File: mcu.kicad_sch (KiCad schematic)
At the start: 30 parts, among them SW1 RESET (RUN to GND), SW2 BOOTSEL (via R24), U20 RP2354B, Y1 12 MHz TAXM12M4RFBCCT2T, CL 1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

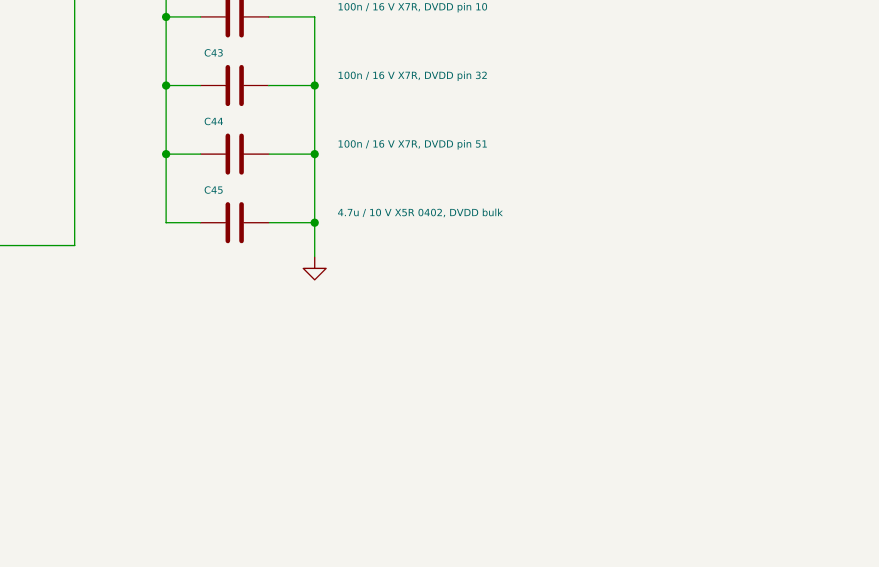
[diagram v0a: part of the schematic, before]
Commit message: Order-ready: core regulator per RP2350 §6.3.8, SWD header, second DVDD cap, README rewrite
Core regulator (U20 / C39 / C45 / L20):
- C39/C45 lands narrowed to 0.46 mm (0.50 mm gap) so VREG_LX passes between
  the pads as in datasheet Fig. 23; local 0.12 mm clearance rule for those
  two footprints only (inside JLC's 3.5 mil four-layer tier)
- In1 GND cutout under L20 and the LX net (Fig. 24); single-point ground
  return with two adjacent vias; B.Cu GND pour tying the SD-cluster vias
- L20 switched to the polarity-marked Abracon AOTA-B201610S3R3-101-T
  (LCSC C42411119) with a silk orientation dot at pad 2 / DVDD
- C81 added: second 4.7 uF on DVDD at the far edge of the package
- U22 BMP581: traces/vias moved out from under the body, mask window opened

Debug: J10 is now a 1x03 2.54 mm THT header wired SWCLK-GND-SWDIO
(Raspberry Pi Debug Probe order); checker, exporter, BOM sources and DFM
rules updated to match.

DFM: courtyard rules relaxed to JLC's body-to-body equivalents (non-overlap
for chip/SOT/SOIC, 0.5 mm courtyard gap IC-to-IC); all 81 findings cleared
without moving parts. DRC 0 errors, 0 unconnected, 0 parity; ERC 0.

Docs: README rewritten around the board, sensor suite, power architecture,
design decisions (external conversion, Q1/D1 OR, sensor LDO, native SD over
PIO, locking microSD socket, fab tier) and the input-power simulation;
DESIGN_SPEC status text brought current; communication-architecture.md
marked historical. Stale root MARV-V2.drl removed (exports live in build/).

Co-Authored-By: Claude Fable 5.1 <noreply@anthropic.com>
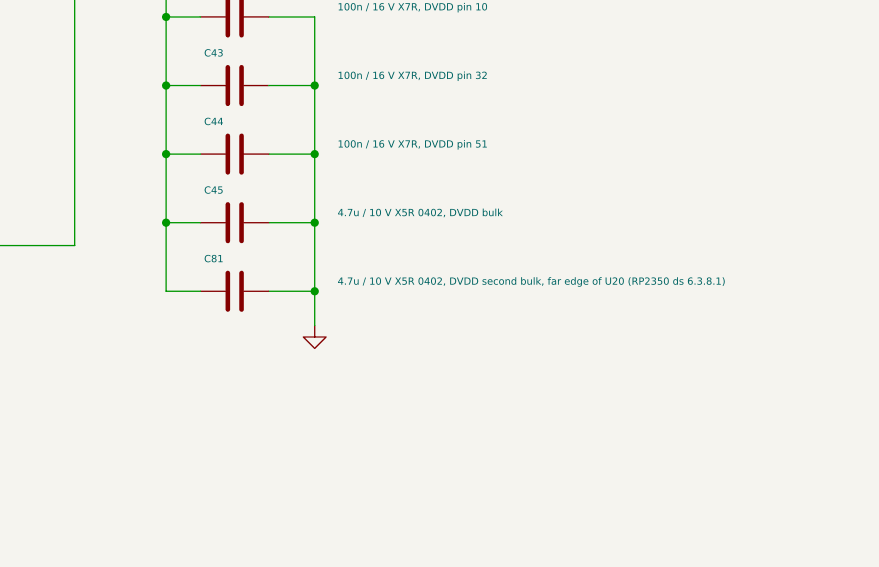
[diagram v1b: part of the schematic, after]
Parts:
- added C81: 4.7u / 10 V X5R 0402, DVDD second bulk, far edge 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, Capacitor_SMD:C_0402_1005Metric, symbol Device:C
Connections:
- net DVDD: now also C81.1
- net GND: now also C81.2
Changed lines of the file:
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@@
 	(wire
 		(pts
-			(xy 367.03 88.9) (xy 367.03 92.71)
+			(xy 367.03 88.9) (xy 367.03 96.52)
 		)
 		(stroke
@@
 	)
 	(symbol
+		(lib_id "Device:C")
+		(at 358.14 96.52 90)
+		(unit 1)
+		(body_style 1)
+		(exclude_from_sim no)
+		(in_bom yes)
+		(on_board yes)
+		(in_pos_files yes)
+		(dnp no)
+		(property "Reference" "C81"
+			(at 354.74 92.92 270)
+			(show_name no)
+			(do_not_autoplace no)
+			(effects
+				(font
+					(size 0.8 0.8)
+				)
+				(justify left)
+			)
+		)
+		(property "Value" "4.7u / 10 V X5R 0402, DVDD second bulk, far edge of U20 (RP2350 ds 6.3.8.1)"
+			(at 369.57 95.42 270)
+			(show_name no)
+			(do_not_autoplace no)
+			(effects
+				(font
+					(size 0.8 0.8)
+				)
+				(justify left)
+			)
+		)
+		(property "Footprint" "Capacitor_SMD:C_0402_1005Metric"
+			(at 358.14 96.52 270)
+			(hide yes)
+			(show_name no)
+			(do_not_autoplace no)
+			(effects
+				(font
+					(size 0.8 0.8)
+				)
+				(justify left)
+			)
+		)
+		(property "Datasheet" ""
+			(at 358.14 96.52 270)
+			(hide yes)
+			(show_name no)
+			(do_not_autoplace no)
+			(effects
+				(font
+					(size 0.8 0.8)
+				)
+				(justify left)
+			)
+		)
+		(property "Description" ""
+			(at 358.14 96.52 0)
+			(show_name no)
+			(do_not_autoplace no)
+			(effects
+				(font
+					(size 1.27 1.27)
+				)
+			)
+		)
+		(property "LCSC" "C23733"
+			(at 358.14 96.52 270)
+			(hide yes)
+			(show_name no)
+			(do_not_autoplace no)
+			(effects
+				(font
+					(size 0.8 0.8)
+				)
+				(justify left)
+			)
+		)
+		(pin "1"
+		)
+		(pin "2"
+		)
+		(instances
+			(project "MARV-V2"
+				(path "/951d7307-88ce-5bfb-b9e0-55612ee5a02b/203e2964-cb5c-592c-ba13-6544f885ad75"
+					(reference "C81")
+					(unit 1)
+				)
+			)
+		)
+	)
+	(symbol
 		(lib_id "Device:L")
 		(at 307.34 55.88 90)
@@
 	(symbol
 		(lib_id "power:GND")
-		(at 367.03 92.71 0)
+		(at 367.03 100.33 0)
 		(unit 1)
 		(body_style 1)
@@
 		(dnp no)
 		(property "Reference" "#PWR027"
-			(at 365.76 88.31 0)
+			(at 365.76 95.93 0)
 			(hide yes)
 			(show_name no)
@@
 		)
 		(property "Value" "GND"
-			(at 365.76 90.51 0)
+			(at 365.76 98.13 0)
 			(hide yes)
 			(show_name no)
@@
 		)
 		(property "Footprint" ""
-			(at 367.03 92.71 0)
+			(at 367.03 100.33 0)
 			(hide yes)
 			(show_name no)
@@
 		)
 		(property "Datasheet" ""
-			(at 367.03 92.71 0)
+			(at 367.03 100.33 0)
 			(hide yes)
 			(show_name no)
@@
 		)
 		(property "Description" ""
-			(at 367.03 92.71 0)
+			(at 367.03 100.33 0)
 			(show_name no)
 			(do_not_autoplace no)
@@
 		)
 	)
+	(wire
+		(pts
+			(xy 367.03 96.52) (xy 367.03 100.33)
+		)
+		(stroke
+			(width 0)
+			(type default)
+		)
+	)
+	(wire
+		(pts
+			(xy 361.95 96.52) (xy 367.03 96.52)
+		)
+		(stroke
+			(width 0)
+			(type default)
+		)
+	)
+	(wire
+		(pts
+			(xy 350.52 88.9) (xy 350.52 96.52)
+		)
+		(stroke
+			(width 0)
+			(type default)
+		)
+	)
+	(wire
+		(pts
+			(xy 350.52 96.52) (xy 354.33 96.52)
+		)
+		(stroke
+			(width 0)
+			(type default)
+		)
+	)
+	(junction
+		(at 367.03 96.52)
+		(diameter 0)
+		(color 0 0 0 0)
+	)
+	(junction
+		(at 350.52 88.9)
+		(diameter 0)
+		(color 0 0 0 0)
+	)
 	(global_label "LED_DATA"
